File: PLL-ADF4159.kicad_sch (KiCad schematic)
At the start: 3 parts, among them J1 6.5V_POWER_IN

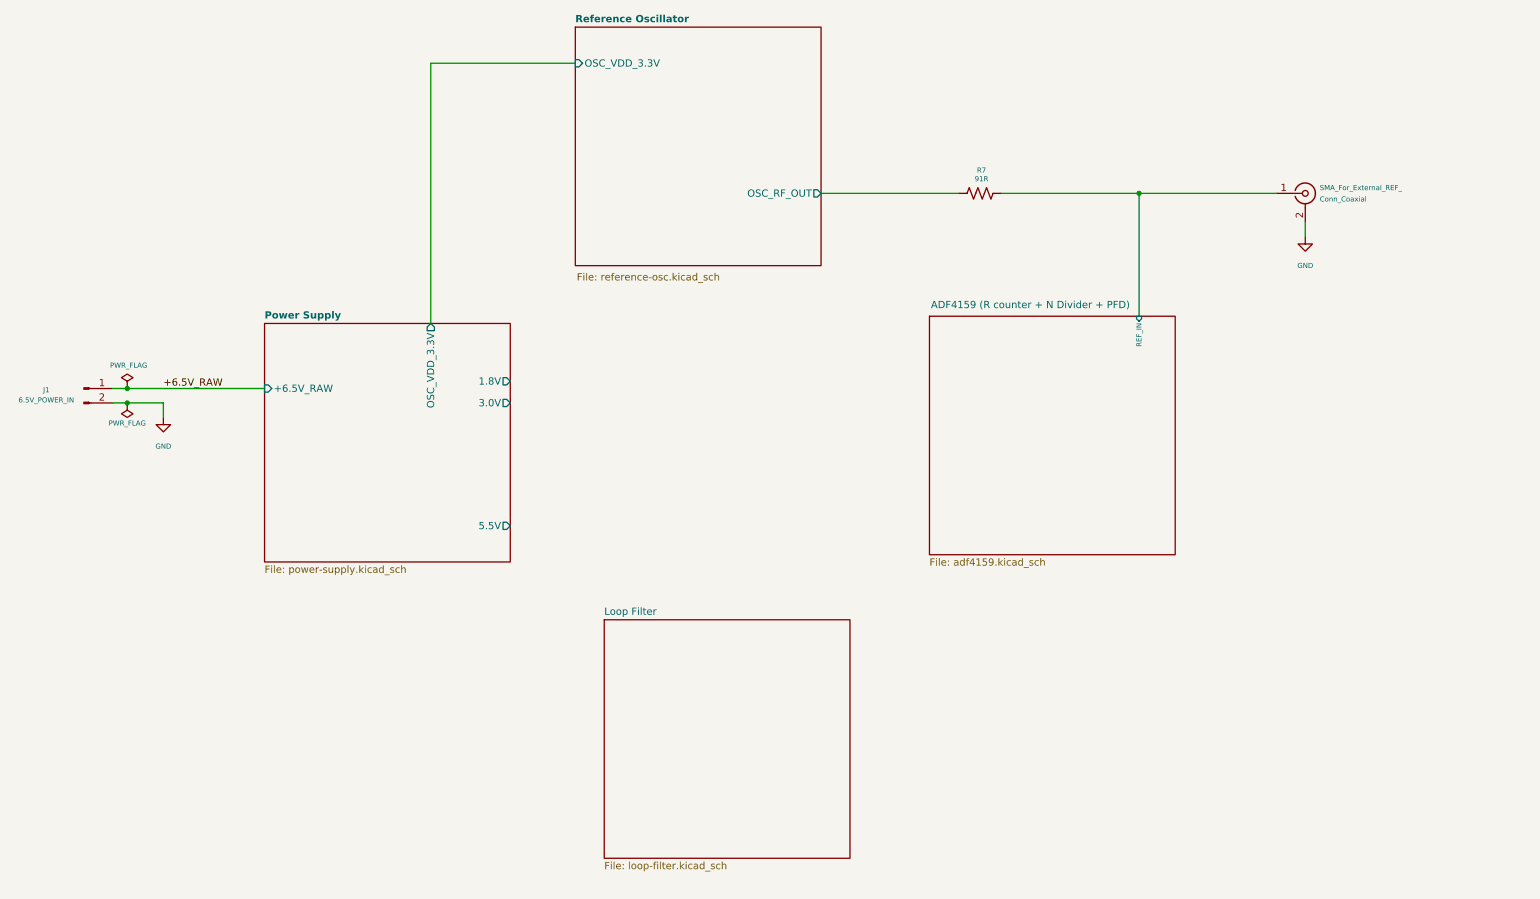
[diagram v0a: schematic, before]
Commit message: Complete Schematic of the PCB
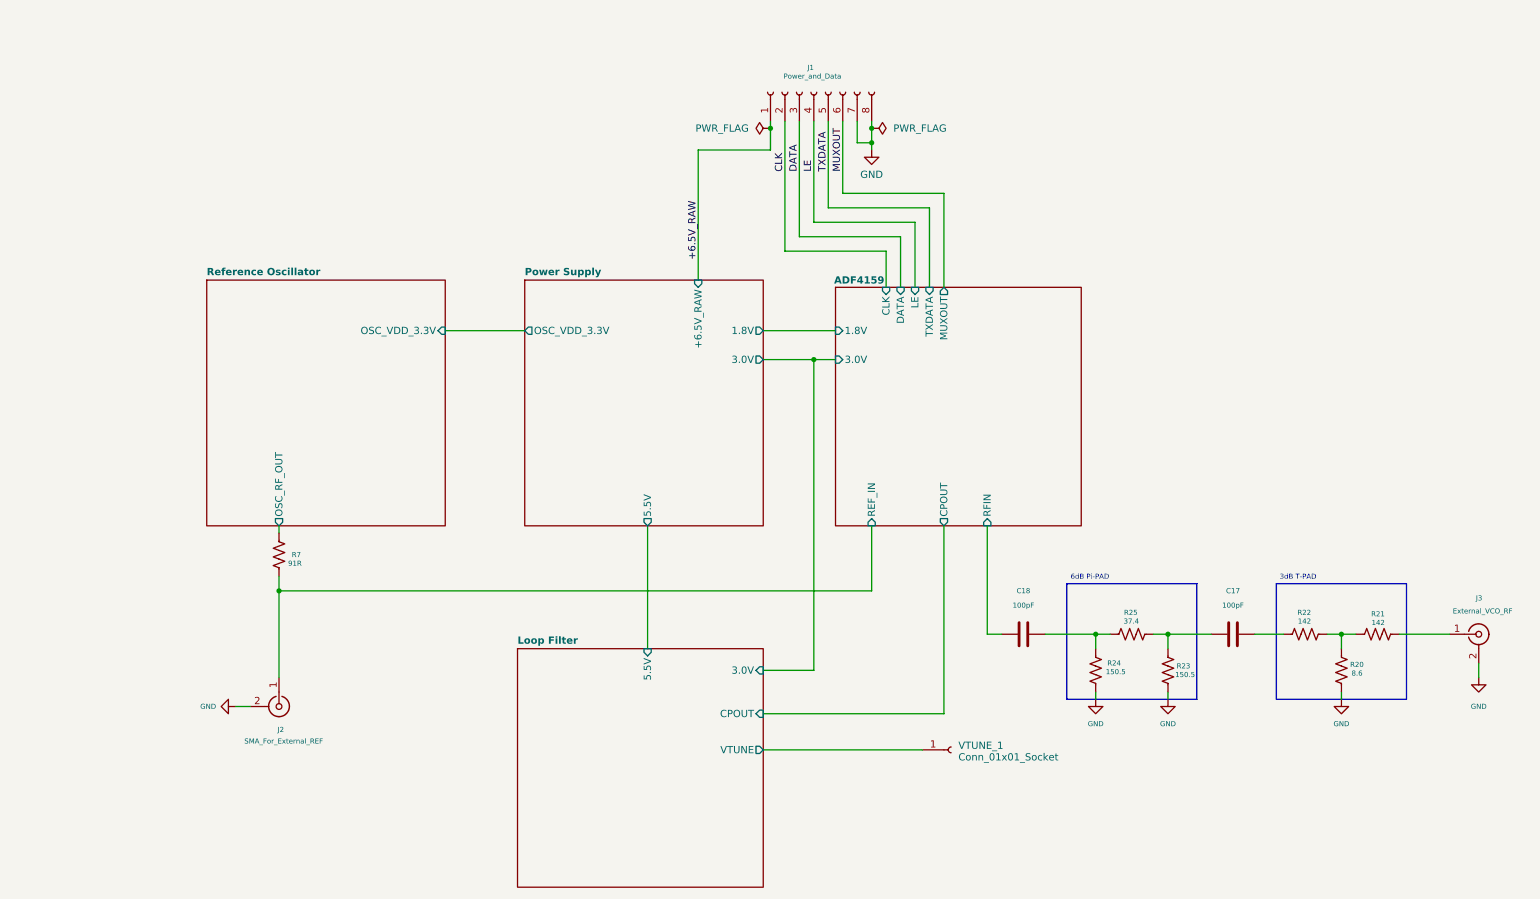
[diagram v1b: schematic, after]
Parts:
- removed J1: 6.5V_POWER_IN, Connector_PinHeader_2.54mm:PinHeader_1x02_P2.54mm_Vertical, symbol Connector:Conn_01x02_Pin
- added C17, C18: 100pF, Capacitor_SMD:C_0402_1005Metric, symbol Device:C
- added J1: Power_and_Data, Connector_PinSocket_2.54mm:PinSocket_2x04_P2.54mm_Vertical, symbol Connector:Conn_01x08_Socket
- added J3: External_VCO_RF, symbol Connector:Conn_Coaxial
- added R20: 8.6, symbol Device:R_US
- added R21, R22: 142, symbol Device:R_US
- added R23, R24: 150.5, symbol Device:R_US
- added R25: 37.4, symbol Device:R_US
- added VTUNE_1: Conn_01x01_Socket, Package_SON:WSON-8-1EP_6x5mm_P1.27mm_EP3.4x4mm, symbol Connector:Conn_01x01_Socket
- J2: renamed from SMA_For_External_REF_; value Conn_Coaxial -> SMA_For_External_REF; footprint CWX813-100.0M_CNW -> CWX813_crystal_osc_100MHz:CWX813-100.0M_CNW
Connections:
- net +6.5V_RAW: now also J1.1 (Pin_1)
- net GND: now also J1.7 (Pin_7), J1.8 (Pin_8), J3.2 (Ext), R20.2, R23.2, R24.2
- new net: C18.2, R24.1, R25.1
- new net: R20.1, R21.1, R22.2
- new net: J3.1 (In), R21.2
- new net: C17.2, R22.1
- new net: C17.1, R23.1, R25.2
- new net ADF4159/RFIN: C18.1
- new net CLK: J1.2 (Pin_2)
- new net DATA: J1.3 (Pin_3)
- new net LE: J1.4 (Pin_4)
- new net Loop Filter/VTUNE: VTUNE_1.1 (Pin_1)
- new net MUXOUT: J1.6 (Pin_6)
- new net TXDATA: J1.5 (Pin_5)
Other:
- sheet ADF4159 (R counter + N Divider + PFD) renamed ADF4159
- sheet ADF4159 ports: added 1.8V, 3.0V, CLK, CPOUT, DATA, LE, MUXOUT, RFIN, TXDATA; removed none
- sheet Loop Filter ports: added 3.0V, 5.5V, CPOUT, VTUNE; removed none
- note added: "3dB T-PAD"
- note added: "6dB Pi-PAD"
- moved on the sheet: J2, R7

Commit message: Remove 0ohm resistors for EN pins and SMA connector for external REFIN
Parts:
- removed J2: SMA_For_External_REF, CWX813_crystal_osc_100MHz:CWX813-100.0M_CNW, symbol Connector:Conn_Coaxial
- J3: footprint (none) -> symbols:SMA_EDGELAUNCH_CUSTOME
- R20, R21, R22, R23, R24, R25, R7: footprint (none) -> Capacitor_SMD:C_0402_1005Metric
- VTUNE_1: footprint Package_SON:WSON-8-1EP_6x5mm_P1.27mm_EP3.4x4mm -> Connector_PinSocket_2.54mm:PinSocket_1x01_P2.54mm_Vertical
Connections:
- net CLK: now also J1.6 (Pin_6); no longer J1.2 (Pin_2)
- net DATA: now also J1.4 (Pin_4); no longer J1.3 (Pin_3)
- net LE: now also J1.2 (Pin_2); no longer J1.4 (Pin_4)
- net MUXOUT: now also J1.3 (Pin_3); no longer J1.6 (Pin_6)

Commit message: Complete and adjust the PCB based on advisor's advice and manufacturer in-stock parts
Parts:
- J3, VTUNE_1: now not fitted; now left out of the parts list
- R20: value 8.6 -> 150; footprint Capacitor_SMD:C_0402_1005Metric -> Resistor_SMD:R_0402_1005Metric
- R21, R22: value 142 -> 8.2; footprint Capacitor_SMD:C_0402_1005Metric -> Resistor_SMD:R_0402_1005Metric; JLCPCB Part # (none) -> C4144; MFR.Part # (none) -> RTT028R20FTH
- R23, R24: value 150.5 -> 150; footprint Capacitor_SMD:C_0402_1005Metric -> Resistor_SMD:R_0402_1005Metric; JLCPCB Part # (none) -> C82683; MFR.Part # (none) -> CRCW0402150RFKED
- R25: value 37.4 -> 39; footprint Capacitor_SMD:C_0402_1005Metric -> Resistor_SMD:R_0402_1005Metric; JLCPCB Part # (none) -> C25110; MFR.Part # (none) -> 0402WGF390JTCE
- R7: value 91R -> 91; footprint Capacitor_SMD:C_0402_1005Metric -> Resistor_SMD:R_0402_1005Metric
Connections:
- net +6.5V_RAW renamed +3.3V_RAW
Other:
- sheet Power Supply ports: added +3.3V_RAW; removed +6.5V_RAW
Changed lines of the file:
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@@
 		)
 	)
-	(label "+6.5V_RAW"
+	(label "+3.3V_RAW"
 		(at 139.7 55.88 270)
 		(effects
@@
 			)
 		)
-		(property "Value" "91R"
+		(property "Value" "91"
 			(at 68.834 119.634 0)
 			(show_name no)
@@
 			)
 		)
-		(property "Footprint" "Capacitor_SMD:C_0402_1005Metric"
+		(property "Footprint" "Resistor_SMD:R_0402_1005Metric"
 			(at 67.056 118.364 90)
 			(hide yes)
@@
 			)
 		)
-		(property "Value" "8.6"
+		(property "Value" "150"
 			(at 254.508 138.938 0)
 			(show_name no)
@@
 			)
 		)
-		(property "Footprint" "Capacitor_SMD:C_0402_1005Metric"
+		(property "Footprint" "Resistor_SMD:R_0402_1005Metric"
 			(at 253.746 138.684 90)
 			(hide yes)
@@
 		(body_style 1)
 		(exclude_from_sim no)
-		(in_bom yes)
-		(on_board yes)
-		(in_pos_files yes)
-		(dnp no)
+		(in_bom no)
+		(on_board yes)
+		(in_pos_files yes)
+		(dnp yes)
 		(property "Reference" "J3"
 			(at 276.352 125.73 0)
@@
 			)
 		)
-		(property "Value" "142"
+		(property "Value" "8.2"
 			(at 247.396 129.794 90)
 			(show_name no)
@@
 			)
 		)
-		(property "Footprint" "Capacitor_SMD:C_0402_1005Metric"
+		(property "Footprint" "Resistor_SMD:R_0402_1005Metric"
 			(at 246.634 131.064 90)
 			(hide yes)
@@
 				(font
 					(size 1.27 1.27)
+				)
+			)
+		)
+		(property "JLCPCB Part #" "C4144"
+			(at 246.38 132.08 90)
+			(hide yes)
+			(show_name no)
+			(do_not_autoplace no)
+			(effects
+				(font
+					(size 0.889 0.889)
+				)
+			)
+		)
+		(property "MFR.Part #" "RTT028R20FTH"
+			(at 246.38 132.08 90)
+			(hide yes)
+			(show_name no)
+			(do_not_autoplace no)
+			(effects
+				(font
+					(size 0.889 0.889)
 				)
 			)
@@
 			)
 		)
-		(property "Value" "150.5"
+		(property "Value" "150"
 			(at 211.328 138.684 0)
 			(show_name no)
@@
 			)
 		)
-		(property "Footprint" "Capacitor_SMD:C_0402_1005Metric"
+		(property "Footprint" "Resistor_SMD:R_0402_1005Metric"
 			(at 210.566 138.684 90)
 			(hide yes)
@@
 				(font
 					(size 1.27 1.27)
+				)
+			)
+		)
+		(property "JLCPCB Part #" "C82683"
+			(at 209.55 138.43 0)
+			(hide yes)
+			(show_name no)
+			(do_not_autoplace no)
+			(effects
+				(font
+					(size 0.889 0.889)
+				)
+			)
+		)
+		(property "MFR.Part #" "CRCW0402150RFKED"
+			(at 209.55 138.43 0)
+			(hide yes)
+			(show_name no)
+			(do_not_autoplace no)
+			(effects
+				(font
+					(size 0.889 0.889)
 				)
 			)
@@
 			)
 		)
-		(property "Value" "150.5"
+		(property "Value" "150"
 			(at 223.52 139.192 0)
 			(show_name no)
@@
 			)
 		)
-		(property "Footprint" "Capacitor_SMD:C_0402_1005Metric"
+		(property "Footprint" "Resistor_SMD:R_0402_1005Metric"
 			(at 223.266 138.684 90)
 			(hide yes)
@@
 			)
 		)
+		(property "JLCPCB Part #" "C82683"
+			(at 222.25 138.43 0)
+			(hide yes)
+			(show_name no)
+			(do_not_autoplace no)
+			(effects
+				(font
+					(size 0.889 0.889)
+				)
+			)
+		)
+		(property "MFR.Part #" "CRCW0402150RFKED"
+			(at 222.25 138.43 0)
+			(hide yes)
+			(show_name no)
+			(do_not_autoplace no)
+			(effects
+				(font
+					(size 0.889 0.889)
+				)
+			)
+		)
 		(pin "2"
 		)
@@
 		(body_style 1)
 		(exclude_from_sim no)
-		(in_bom yes)
-		(on_board yes)
-		(in_pos_files yes)
-		(dnp no)
+		(in_bom no)
+		(on_board yes)
+		(in_pos_files yes)
+		(dnp yes)
 		(property "Reference" "VTUNE_1"
 			(at 185.42 151.638 0)
@@
 			)
 		)
-		(property "Value" "142"
+		(property "Value" "8.2"
 			(at 260.35 130.048 90)
 			(show_name no)
@@
 			)
 		)
-		(property "Footprint" "Capacitor_SMD:C_0402_1005Metric"
+		(property "Footprint" "Resistor_SMD:R_0402_1005Metric"
 			(at 259.334 131.064 90)
 			(hide yes)
@@
 			)
 		)
+		(property "JLCPCB Part #" "C4144"
+			(at 259.08 132.08 90)
+			(hide yes)
+			(show_name no)
+			(do_not_autoplace no)
+			(effects
+				(font
+					(size 0.889 0.889)
+				)
+			)
+		)
+		(property "MFR.Part #" "RTT028R20FTH"
+			(at 259.08 132.08 90)
+			(hide yes)
+			(show_name no)
+			(do_not_autoplace no)
+			(effects
+				(font
+					(size 0.889 0.889)
+				)
+			)
+		)
 		(pin "2"
 		)
@@
 			)
 		)
-		(property "Value" "37.4"
+		(property "Value" "39"
 			(at 217.17 129.794 90)
 			(show_name no)
@@
 			)
 		)
-		(property "Footprint" "Capacitor_SMD:C_0402_1005Metric"
+		(property "Footprint" "Resistor_SMD:R_0402_1005Metric"
 			(at 216.154 131.064 90)
 			(hide yes)
@@
 				(font
 					(size 1.27 1.27)
+				)
+			)
+		)
+		(property "JLCPCB Part #" "C25110"
+			(at 215.9 132.08 90)
+			(hide yes)
+			(show_name no)
+			(do_not_autoplace no)
+			(effects
+				(font
+					(size 0.889 0.889)
+				)
+			)
+		)
+		(property "MFR.Part #" "0402WGF390JTCE"
+			(at 215.9 132.08 90)
+			(hide yes)
+			(show_name no)
+			(do_not_autoplace no)
+			(effects
+				(font
+					(size 0.889 0.889)
 				)
 			)
@@
 			)
 		)
-		(pin "+6.5V_RAW" input
+		(pin "+3.3V_RAW" input
 			(at 139.7 69.85 90)
 			(effects
